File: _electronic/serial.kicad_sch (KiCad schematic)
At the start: 14 parts

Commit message: organized electronics folder
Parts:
- C_SER1, C_SER4: value 0.1uF 10V -> 0.1uF 50V; # CGA3E2X7R1H104K080AA -> C1608X7R1H104K080AA
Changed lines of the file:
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@@
       (effects (font (size 1.27 1.27)) (justify left))
     )
-    (property "Value" "0.1uF 10V" (id 1) (at 105.41 133.35 0)
+    (property "Value" "0.1uF 50V" (id 1) (at 105.41 133.35 0)
       (effects (font (size 1.27 1.27)) (justify left))
     )
@@
       (effects (font (size 1.27 1.27)) hide)
     )
-    (property "#" "CGA3E2X7R1H104K080AA" (id 4) (at 104.14 132.08 0)
+    (property "#" "C1608X7R1H104K080AA" (id 4) (at 104.14 132.08 0)
       (effects (font (size 1.27 1.27)) (justify left) hide)
     )
@@
       (effects (font (size 1.27 1.27)) (justify left))
     )
-    (property "Value" "0.1uF 10V" (id 1) (at 87.63 133.35 0)
+    (property "Value" "0.1uF 50V" (id 1) (at 87.63 133.35 0)
       (effects (font (size 1.27 1.27)) (justify left))
     )
@@
       (effects (font (size 1.27 1.27)) hide)
     )
-    (property "#" "CGA3E2X7R1H104K080AA" (id 4) (at 83.82 132.08 0)
-      (effects (font (size 1.27 1.27)) hide)
-    )
+    (property "#" "C1608X7R1H104K080AA" (id 4) (at 83.82 132.08 0)
+      (effects (font (size 1.27 1.27)) hide)
+    )

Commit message: revised pcb: direct power, leds, ftdi w/o 3v3
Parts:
- removed C_SER1: 0.1uF 50V, Capacitor_SMD:C_0603_1608Metric_Pad1.08x0.95mm_HandSolder, symbol Device:C
- removed JP_SER1, JP_SER3: Bridged, Jumper:SolderJumper-2_P1.3mm_Bridged2Bar_Pad1.0x1.5mm, symbol Jumper:SolderJumper_2_Bridged
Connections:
- net 3V3 IN: no longer U_SER1.13 (3V3OUT), U_SER1.14 (~{RESET})
- net RXD OUT: now also U_SER1.4 (RXD)
- net TXD OUT: now also U_SER1.20 (TXD)
- new net: U_SER1.13 (3V3OUT), U_SER1.14 (~{RESET})
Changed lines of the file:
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@@
     (company "Andrei Speridiao")
-  )
-  (junction (at 130.81 77.47) (diameter 0) (color 0 0 0 0)
   )
   (junction (at 149.86 116.84) (diameter 0) (color 0 0 0 0)
@@
     (stroke (width 0) (type default) (color 0 0 0 0))
   )
-  (wire (pts (xy 83.82 135.89) (xy 83.82 137.16))
-    (stroke (width 0) (type default) (color 0 0 0 0))
-  )
   (wire (pts (xy 129.54 87.63) (xy 132.08 87.63))
     (stroke (width 0) (type default) (color 0 0 0 0))
   )
-  (wire (pts (xy 189.23 80.01) (xy 196.85 80.01))
-    (stroke (width 0) (type default) (color 0 0 0 0))
-  )
   (wire (pts (xy 180.34 121.92) (xy 185.42 121.92))
     (stroke (width 0) (type default) (color 0 0 0 0))
@@
     (stroke (width 0) (type default) (color 0 0 0 0))
   )
-  (wire (pts (xy 130.81 67.31) (xy 130.81 77.47))
-    (stroke (width 0) (type default) (color 0 0 0 0))
-  )
-  (wire (pts (xy 181.61 80.01) (xy 167.64 80.01))
+  (wire (pts (xy 167.64 80.01) (xy 196.85 80.01))
     (stroke (width 0) (type default) (color 0 0 0 0))
   )
@@
     (stroke (width 0) (type default) (color 0 0 0 0))
   )
-  (wire (pts (xy 182.88 77.47) (xy 196.85 77.47))
-    (stroke (width 0) (type default) (color 0 0 0 0))
-  )
   (wire (pts (xy 149.86 119.38) (xy 149.86 116.84))
     (stroke (width 0) (type default) (color 0 0 0 0))
@@
     (stroke (width 0) (type default) (color 0 0 0 0))
   )
+  (wire (pts (xy 130.81 67.31) (xy 130.81 74.93))
+    (stroke (width 0) (type default) (color 0 0 0 0))
+  )
   (wire (pts (xy 167.64 105.41) (xy 177.8 105.41))
     (stroke (width 0) (type default) (color 0 0 0 0))
@@
     (stroke (width 0) (type default) (color 0 0 0 0))
   )
-  (wire (pts (xy 175.26 77.47) (xy 167.64 77.47))
-    (stroke (width 0) (type default) (color 0 0 0 0))
-  )
-  (wire (pts (xy 83.82 125.73) (xy 83.82 128.27))
+  (wire (pts (xy 167.64 77.47) (xy 196.85 77.47))
     (stroke (width 0) (type default) (color 0 0 0 0))
   )
@@
   )
   (hierarchical_label "VBUS IN" (shape input) (at 119.38 125.73 90)
-    (effects (font (size 1.27 1.27)) (justify left))
-  )
-  (hierarchical_label "3V3 IN" (shape input) (at 83.82 125.73 90)
     (effects (font (size 1.27 1.27)) (justify left))
   )
@@
     (pin "2")
   )
-  (symbol (lib_id "Jumper:SolderJumper_2_Bridged") (at 179.07 77.47 0) (unit 1)
-    (in_bom yes) (on_board yes)
-    (property "Reference" "JP_SER3" (id 0) (at 177.8 76.2 0)
-      (effects (font (size 1.27 1.27)) (justify right))
-    )
-    (property "Value" "Bridged" (id 1) (at 176.53 74.93 0)
-      (effects (font (size 1.27 1.27)) (justify left) hide)
-    )
-    (property "Footprint" "Jumper:SolderJumper-2_P1.3mm_Bridged2Bar_Pad1.0x1.5mm" (id 2) (at 179.07 77.47 0)
-      (effects (font (size 1.27 1.27)) hide)
-    )
-    (property "Datasheet" "xxx" (id 3) (at 179.07 77.47 0)
-      (effects (font (size 1.27 1.27)) hide)
-    )
-    (property "#" "xxx" (id 4) (at 179.07 77.47 0)
-      (effects (font (size 1.27 1.27)) hide)
-    )
-    (property "Description" "Solder jumper" (id 5) (at 179.07 77.47 0)
-      (effects (font (size 1.27 1.27)) hide)
-    )
-    (property "Group" "Serial" (id 6) (at 179.07 77.47 0)
-      (effects (font (size 1.27 1.27)) hide)
-    )
-    (property "Mouser" "OK" (id 7) (at 179.07 77.47 0)
-      (effects (font (size 1.27 1.27)) hide)
-    )
-    (pin "1")
-    (pin "2")
-  )
   (symbol (lib_id "Device:R") (at 185.42 116.84 0) (unit 1)
     (in_bom yes) (on_board yes)
@@
     )
     (pin "1")
-  )
-  (symbol (lib_id "Jumper:SolderJumper_2_Bridged") (at 185.42 80.01 0) (unit 1)
-    (in_bom yes) (on_board yes)
-    (property "Reference" "JP_SER1" (id 0) (at 186.69 78.74 0)
-      (effects (font (size 1.27 1.27)) (justify left))
-    )
-    (property "Value" "Bridged" (id 1) (at 182.88 77.47 0)
-      (effects (font (size 1.27 1.27)) (justify left) hide)
-    )
-    (property "Footprint" "Jumper:SolderJumper-2_P1.3mm_Bridged2Bar_Pad1.0x1.5mm" (id 2) (at 185.42 80.01 0)
-      (effects (font (size 1.27 1.27)) hide)
-    )
-    (property "Datasheet" "xxx" (id 3) (at 185.42 80.01 0)
-      (effects (font (size 1.27 1.27)) hide)
-    )
-    (property "#" "xxx" (id 4) (at 185.42 80.01 0)
-      (effects (font (size 1.27 1.27)) hide)
-    )
-    (property "Description" "Solder jumper" (id 5) (at 185.42 80.01 0)
-      (effects (font (size 1.27 1.27)) hide)
-    )
-    (property "Group" "Serial" (id 6) (at 185.42 80.01 0)
-      (effects (font (size 1.27 1.27)) hide)
-    )
-    (property "Mouser" "OK" (id 7) (at 185.42 80.01 0)
-      (effects (font (size 1.27 1.27)) hide)
-    )
-    (pin "1")
-    (pin "2")
-  )
-  (symbol (lib_id "Device:C") (at 83.82 132.08 0) (unit 1)
-    (in_bom yes) (on_board yes)
-    (property "Reference" "C_SER1" (id 0) (at 87.63 130.81 0)
-      (effects (font (size 1.27 1.27)) (justify left))
-    )
-    (property "Value" "0.1uF 50V" (id 1) (at 87.63 133.35 0)
-      (effects (font (size 1.27 1.27)) (justify left))
-    )
-    (property "Footprint" "Capacitor_SMD:C_0603_1608Metric_Pad1.08x0.95mm_HandSolder" (id 2) (at 84.7852 135.89 0)
-      (effects (font (size 1.27 1.27)) hide)
-    )
-    (property "Datasheet" "https://product.tdk.com/system/files/dam/doc/product/capacitor/ceramic/mlcc/catalog/mlcc_automotive_general_en.pdf?ref_disty=mouser" (id 3) (at 83.82 132.08 0)
-      (effects (font (size 1.27 1.27)) hide)
-    )
-    (property "#" "C1608X7R1H104K080AA" (id 4) (at 83.82 132.08 0)
-      (effects (font (size 1.27 1.27)) hide)
-    )
-    (property "Description" "Decouple" (id 5) (at 83.82 132.08 0)
-      (effects (font (size 1.27 1.27)) hide)
-    )
-    (property "Group" "Serial" (id 6) (at 83.82 132.08 0)
-      (effects (font (size 1.27 1.27)) hide)
-    )
-    (property "Mouser" "OK" (id 7) (at 83.82 132.08 0)
-      (effects (font (size 1.27 1.27)) hide)
-    )
-    (pin "1")
-    (pin "2")
   )
   (symbol (lib_id "Device:LED") (at 195.58 107.95 90) (unit 1)
@@
       (effects (font (size 1.27 1.27)) hide)
     )
-    (pin "1")
-  )
-  (symbol (lib_id "power:GNDREF") (at 83.82 137.16 0) (unit 1)
-    (in_bom yes) (on_board yes) (fields_autoplaced)
-    (property "Reference" "#PWR0183" (id 0) (at 83.82 143.51 0)
-      (effects (font (size 1.27 1.27)) hide)
-    )
-    (property "Value" "GNDREF" (id 1) (at 83.82 142.24 0)
-      (effects (font (size 1.27 1.27)) hide)
-    )
-    (property "Footprint" "" (id 2) (at 83.82 137.16 0)
-      (effects (font (size 1.27 1.27)) hide)
-    )
-    (property "Datasheet" "" (id 3) (at 83.82 137.16 0)
-      (effects (font (size 1.27 1.27)) hide)
-    )

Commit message: v1 pcb
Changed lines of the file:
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@@
+    (stroke (width 0) (type default) (color 0 0 0 0))
+  )
+  (wire (pts (xy 152.4 64.77) (xy 152.4 69.85))
     (stroke (width 0) (type default) (color 0 0 0 0))
   )
   (wire (pts (xy 170.18 95.25) (xy 167.64 95.25))
-    (stroke (width 0) (type default) (color 0 0 0 0))
-  )
-  (wire (pts (xy 152.4 67.31) (xy 152.4 69.85))
     (stroke (width 0) (type default) (color 0 0 0 0))
   )
@@
     (effects (font (size 1.27 1.27)) (justify right))
   )
-  (hierarchical_label "3V3 IN" (shape input) (at 152.4 67.31 90)
+  (hierarchical_label "3V3 IN" (shape input) (at 152.4 64.77 90)
     (effects (font (size 1.27 1.27)) (justify left))
   )

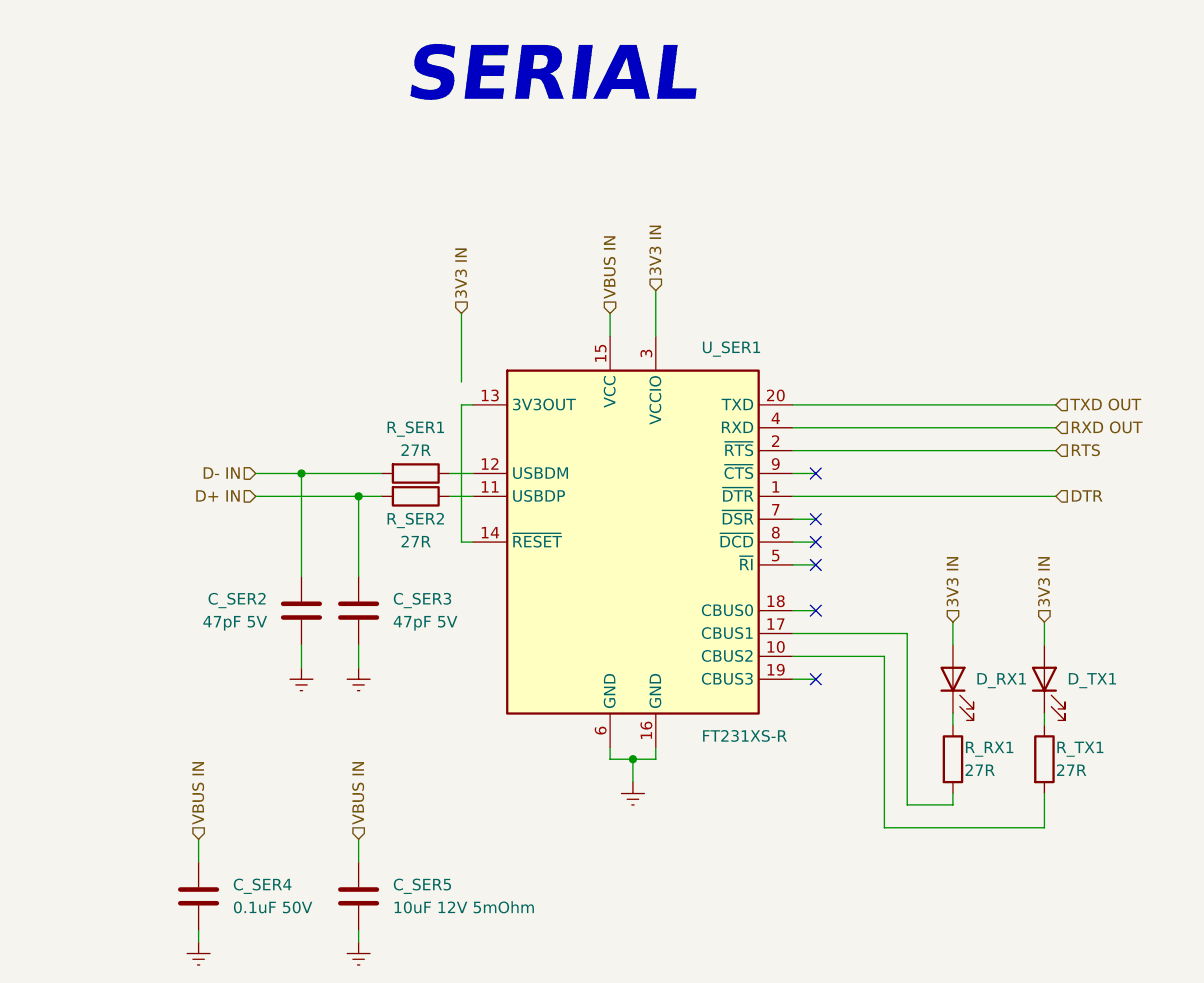
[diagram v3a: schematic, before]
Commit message: led resistor revision, b.o.m. and pcb anotation
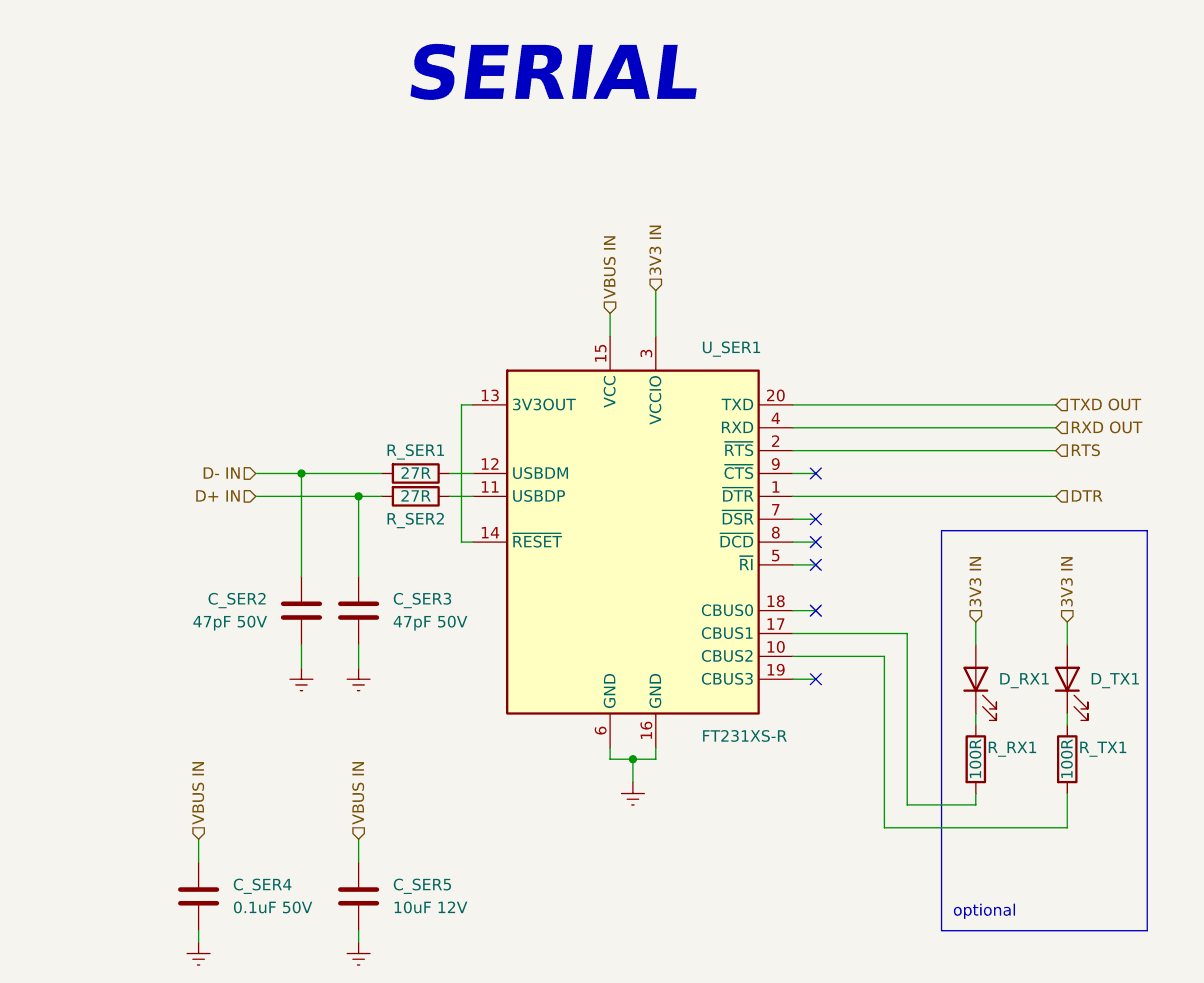
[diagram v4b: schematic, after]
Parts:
- C_SER2, C_SER3: value 47pF 5V -> 47pF 50V
- C_SER5: value 10uF 12V 5mOhm -> 10uF 12V; # C1608X5R1E106M080AC -> GRM188Z71A106KA73D
- R_RX1, R_TX1: value 27R -> 100R; # CMP0603-FX-27R0ELF -> ERJ-3EKF1000V
- R_SER1, R_SER2: # CMP0603-FX-27R0ELF -> ERJ-3EKF27R0V
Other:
- note added: "optional"
- moved on the sheet: D_RX1, D_TX1, R_RX1, R_TX1

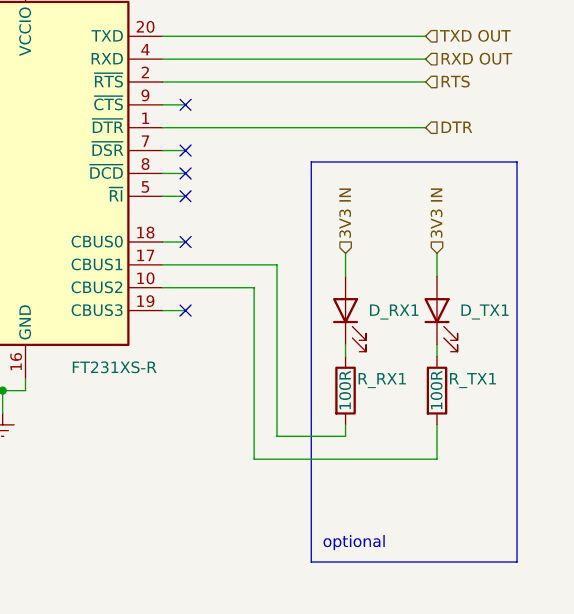
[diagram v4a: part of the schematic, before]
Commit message: schematics and pcb cleanup
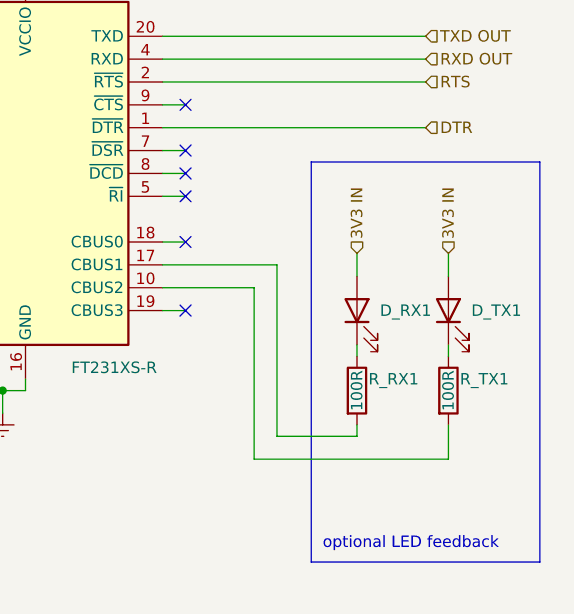
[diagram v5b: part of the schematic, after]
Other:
- note added: "optional LED feedback"
- note removed: "optional"
- title: E-TKT -> E-TKT v1.0
- moved on the sheet: D_RX1, D_TX1, R_RX1, R_TX1
